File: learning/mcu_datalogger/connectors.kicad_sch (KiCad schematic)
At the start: 0 parts

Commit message: Finished the schematic design
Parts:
- added J1: Conn_01x09_Pin, Connector_PinHeader_2.54mm:PinHeader_1x09_P2.54mm_Vertical, symbol Connector:Conn_01x09_Pin
- added J2, J3: Conn_01x04_Pin, Connector_PinHeader_2.54mm:PinHeader_1x04_P2.54mm_Vertical, symbol Connector:Conn_01x04_Pin
- added J4: Conn_02x03_Odd_Even, Connector_PinHeader_2.54mm:PinHeader_2x03_P2.54mm_Vertical, symbol Connector_Generic:Conn_02x03_Odd_Even
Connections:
- new net D2: J1.1 (Pin_1)
- new net D3: J1.2 (Pin_2)
- new net D4: J1.3 (Pin_3)
- new net D5: J1.4 (Pin_4)
- new net D6: J1.5 (Pin_5)
- new net D7: J1.6 (Pin_6)
- new net D8: J1.7 (Pin_7)
- new net GND: J1.8 (Pin_8), J2.1 (Pin_1), J3.1 (Pin_1), J4.6 (Pin_6)
- new net MISO: J4.1 (Pin_1)
- new net MOSI: J4.4 (Pin_4)
- new net RESET: J4.5 (Pin_5)
- new net RX: J3.3 (Pin_3)
- new net SCK: J2.4 (Pin_4), J4.3 (Pin_3)
- new net SDA: J2.3 (Pin_3)
- new net TX: J3.4 (Pin_4)
- new net Vcc: J1.9 (Pin_9), J2.2 (Pin_2), J3.2 (Pin_2), J4.2 (Pin_2)
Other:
- note added: "Connectors"

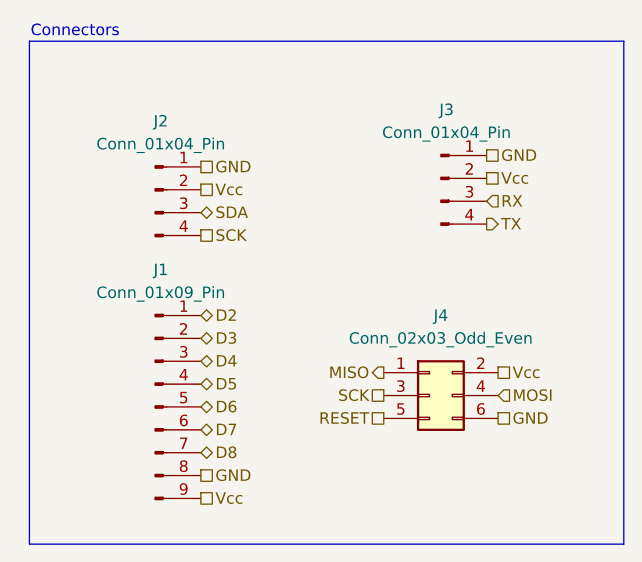
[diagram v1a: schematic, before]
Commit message: Finished mcu datalogger schematic design
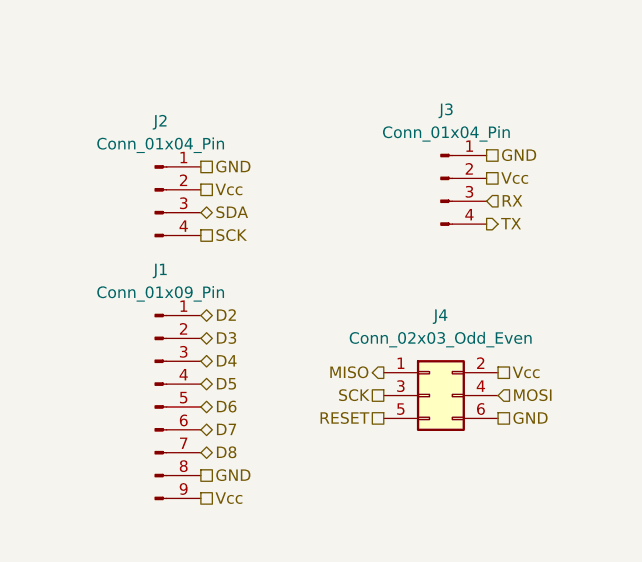
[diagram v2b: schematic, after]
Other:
- note removed: "Connectors"
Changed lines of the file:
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@@
 	(generator_version "9.0")
 	(paper "A4")
-	(rectangle
-		(start 99.06 63.5)
-		(end 165.1 119.38)
-		(stroke
-			(width 0)
-			(type default)
-		)
-		(fill
-			(type none)
-		)
-	)
-	(text "Connectors"
-		(exclude_from_sim no)
-		(at 104.14 62.484 0)
-		(effects
-			(font
-				(size 1.27 1.27)
-			)
-		)
-	)
 	(hierarchical_label "RX"
 		(shape input)
@@
 		(instances
 			(project "connectors"
+				(path "/58e3bb87-6680-4c5a-ab7a-66531b46fe94/437b2a52-4fcd-403a-be21-fbd36d934856"
+					(reference "J2")
+					(unit 1)
+				)
+			)
+			(project "connectors"
 				(path "/c28cf371-00a5-4adb-a3d0-0b3e9f5dd3b8"
 					(reference "J2")
@@
 		(instances
 			(project "connectors"
+				(path "/58e3bb87-6680-4c5a-ab7a-66531b46fe94/437b2a52-4fcd-403a-be21-fbd36d934856"
+					(reference "J3")
+					(unit 1)
+				)
+			)
+			(project "connectors"
 				(path "/c28cf371-00a5-4adb-a3d0-0b3e9f5dd3b8"
 					(reference "J3")
@@
 		(instances
 			(project "connectors"
+				(path "/58e3bb87-6680-4c5a-ab7a-66531b46fe94/437b2a52-4fcd-403a-be21-fbd36d934856"
+					(reference "J4")
+					(unit 1)
+				)
+			)
+			(project "connectors"
 				(path "/c28cf371-00a5-4adb-a3d0-0b3e9f5dd3b8"
 					(reference "J4")
@@
 		(instances
 			(project "connectors"
+				(path "/58e3bb87-6680-4c5a-ab7a-66531b46fe94/437b2a52-4fcd-403a-be21-fbd36d934856"
+					(reference "J1")
+					(unit 1)
+				)
+			)
+			(project "connectors"
 				(path "/c28cf371-00a5-4adb-a3d0-0b3e9f5dd3b8"
 					(reference "J1")
@@
 		)
 	)
-	(sheet_instances
-		(path "/"
-			(page "1")
-		)
-	)
-	(embedded_fonts no)
 )
